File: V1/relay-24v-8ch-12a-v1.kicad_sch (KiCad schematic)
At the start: 47 parts, among them J1 DB141V-2.54-2P, J2 DB141V-2.54-4P, J3 DB141V-2.54-4P, J4 DB142V-5.08-4P, J5 DB142V-5.08-4P, J6 DB142V-5.08-4P, J7 DB142V-5.08-4P, K1 G5PZ-1A, K2 G5PZ-1A, K3 G5PZ-1A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

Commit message: Review before fabrication
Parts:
- K1, K2, K3, K4, K5, K6, K7, K8: JLCPCB BOM 0 -> 1; LCSC Part # (none) -> C6719448; Mfr PN G5PZ-1A -> G5PZ-1A-E DC24V; Vendor Mouser -> JLCPCB; Vendor PN 653-G5PZ-1ADC24 -> C6719448
- R1, R2, R3, R4, R5, R6, R7, R8: value 6k8/100mW -> 10k/100mW; LCSC Part # C23212 -> C25804; Mfr Uniroyal -> UNI-ROYAL(Uniroyal Elec); Mfr PN 0603WAF6801T5E -> 0603WAF1002T5E; Vendor PN C23212 -> C25804
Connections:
- net IN7: now reaches D13.1 (K), D14.2 (A), J3.2 (Pin_2), K7.4
- net LED7: now reaches D13.2 (A), R7.2
- net OUT5PW: now reaches J6.1 (Pin_1), K5.2, RV5.1
- net OUT5LD: now reaches J6.2 (Pin_2), K5.3, RV5.2
- net OUT1PW: now reaches J4.1 (Pin_1), K1.2, RV1.1
- net OUT1LD: now reaches J4.2 (Pin_2), K1.3, RV1.2
- net OUT2PW: now reaches J4.3 (Pin_3), K2.2, RV2.1
- net OUT2LD: now reaches J4.4 (Pin_4), K2.3, RV2.2
- net OUT3PW: now reaches J5.1 (Pin_1), K3.2, RV3.1
- net OUT3LD: now reaches J5.2 (Pin_2), K3.3, RV3.2
- net OUT4PW: now reaches J5.3 (Pin_3), K4.2, RV4.1
- net OUT4LD: now reaches J5.4 (Pin_4), K4.3, RV4.2
- net IN4: now reaches D7.1 (K), D8.2 (A), J2.1 (Pin_1), K4.4
- net LED4: now reaches D7.2 (A), R4.2
- net OUT7PW: now reaches J7.1 (Pin_1), K7.2, RV7.1
- net OUT7LD: now reaches J7.2 (Pin_2), K7.3, RV7.2
- net IN3: now reaches D5.1 (K), D6.2 (A), J2.2 (Pin_2), K3.4
- net LED6: now reaches D11.2 (A), R6.2
- net IN1: now reaches D1.1 (K), D2.2 (A), J2.4 (Pin_4), K1.4
- net IN6: now reaches D11.1 (K), D12.2 (A), J3.3 (Pin_3), K6.4
- net LED8: now reaches D15.2 (A), R8.2
- net OUT6PW: now reaches J6.3 (Pin_3), K6.2, RV6.1
- net OUT6LD: now reaches J6.4 (Pin_4), K6.3, RV6.2
- net IN5: now reaches D10.2 (A), D9.1 (K), J3.4 (Pin_4), K5.4
- net LED5: now reaches D9.2 (A), R5.2
- net LED1: now reaches D1.2 (A), R1.2
- net IN2: now reaches D3.1 (K), D4.2 (A), J2.3 (Pin_3), K2.4
- net LED3: now reaches D5.2 (A), R3.2
- net IN8: now reaches D15.1 (K), D16.2 (A), J3.1 (Pin_1), K8.4
- net OUT8PW: now reaches J7.3 (Pin_3), K8.2, RV8.1
- net OUT8LD: now reaches J7.4 (Pin_4), K8.3, RV8.2
- net LED2: now reaches D3.2 (A), R2.2
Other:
- moved on the sheet: D1, D11, D12, D13, D15, D16, D3, D4, D5, D7, D8, D9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

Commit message: Revising before manufacturing.
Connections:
- net OUT1PW renamed OUT1LN
- net OUT2PW renamed OUT2LN
- net OUT3PW renamed OUT3LN
- net OUT4PW renamed OUT4LN
- net OUT5PW renamed OUT5LN
- net OUT6PW renamed OUT6LN
- net OUT7PW renamed OUT7LN
- net OUT8PW renamed OUT8LN
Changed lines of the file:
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@@
 		)
 	)
-	(label "OUT6PW"
+	(label "OUT6LN"
 		(at 240.03 97.79 0)
 		(effects
@@
 		)
 	)
-	(label "OUT5PW"
+	(label "OUT5LN"
 		(at 240.03 92.71 0)
 		(effects
@@
 		)
 	)
-	(label "OUT7PW"
+	(label "OUT7LN"
 		(at 240.03 130.81 0)
 		(effects
@@
 		)
 	)
-	(label "OUT3PW"
+	(label "OUT3LN"
 		(at 240.03 54.61 0)
 		(effects
@@
 		)
 	)
-	(label "OUT2PW"
+	(label "OUT2LN"
 		(at 240.03 21.59 0)
 		(effects
@@
 		)
 	)
-	(label "OUT4PW"
+	(label "OUT4LN"
 		(at 240.03 59.69 0)
 		(effects
@@
 		)
 	)
-	(label "OUT1PW"
+	(label "OUT1LN"
 		(at 240.03 16.51 0)
 		(effects
@@
 		)
 	)
-	(label "OUT8PW"
+	(label "OUT8LN"
 		(at 240.03 135.89 0)
 		(effects

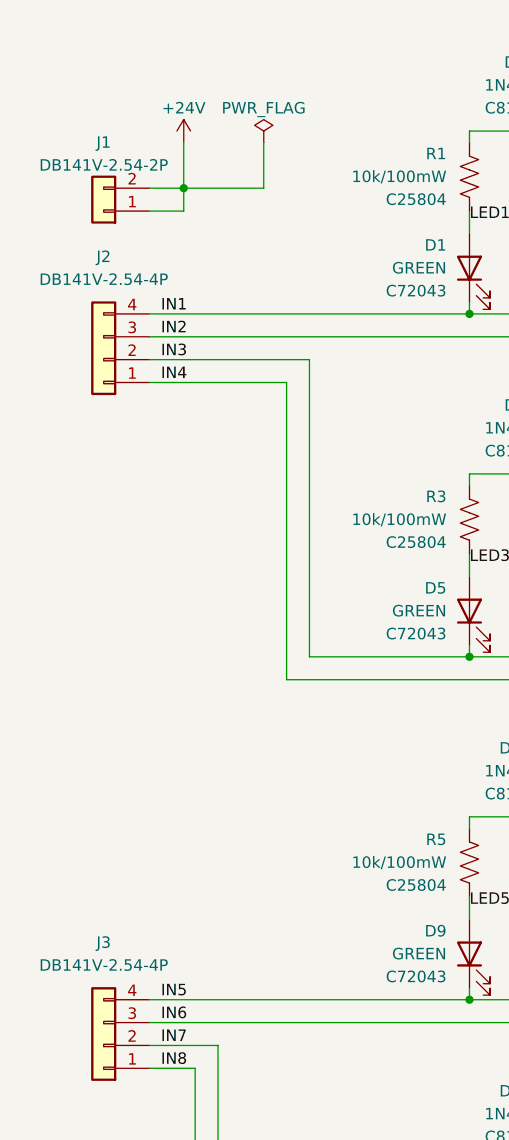
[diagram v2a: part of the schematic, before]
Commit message: Replaced input terminal blocks for 3.5mm pitch.
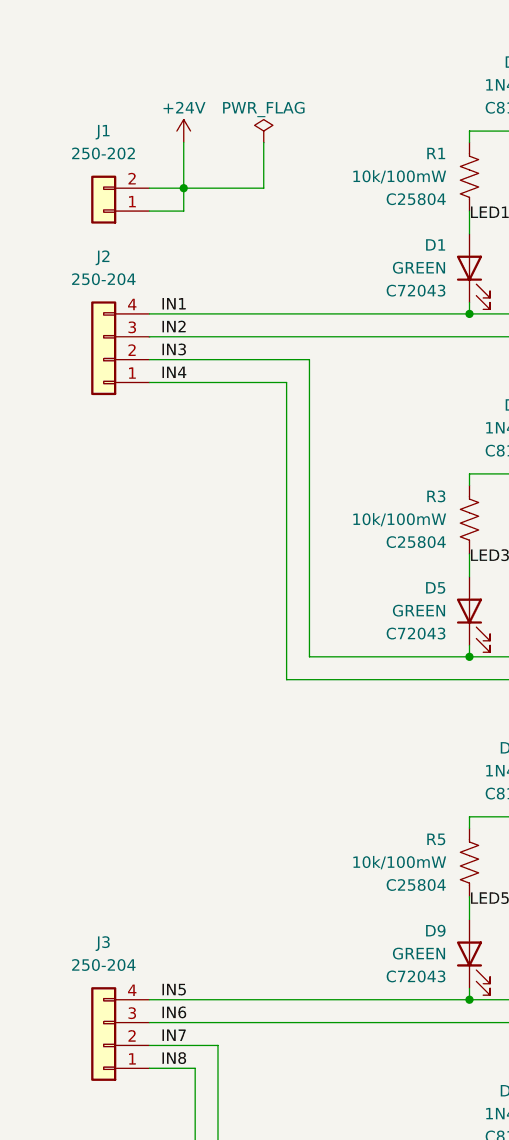
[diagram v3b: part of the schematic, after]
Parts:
- J1: value DB141V-2.54-2P -> 250-202; footprint Tales:TerminalBlock_Dibo_DB141V-2.54-2P_1x02_P2.54mm_Vertical -> Tales:TerminalBlock_Wago_250-202_1x02_P3.5mm_45Degree; LCSC Part # (none) -> C2765061; Mfr (none) -> Wago; Mfr PN (none) -> 250-202; Vendor PN (none) -> C2765061
- J2, J3: value DB141V-2.54-4P -> 250-204; footprint Tales:TerminalBlock_Dibo_DB141V-2.54-4P_1x04_P2.54mm_Vertical -> Tales:TerminalBlock_Wago_250-204_1x04_P3.5mm_45Degree; LCSC Part # (none) -> C2765063; Mfr (none) -> Wago; Mfr PN (none) -> 250-204; Vendor PN (none) -> C2765063
